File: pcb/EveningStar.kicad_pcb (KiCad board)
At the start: 2 copper layers, 134 parts, among them J1 3V3_JMP, J2 Connector, USB-TYPE-C-16P, J3 ESPPROG, J4 RJ45_Hanrun_HR911105A_Horizon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, Q1 SQ2308CES-T1_GE3-HXY, SW1 RST_SW, SW2 BOOT_SW, SW3 CFG_SW, U1 AMS1117S-5.0, U2 SN74HC132DR, U3 ISO6721RBDR, U4 DC-005H-D020, U5 LMR16010, U6 AHT20_C2757850, U7 TLV803SDBZR, U8 ESP32-C6-MINI-1, U9 W5500, Y1 25MHz

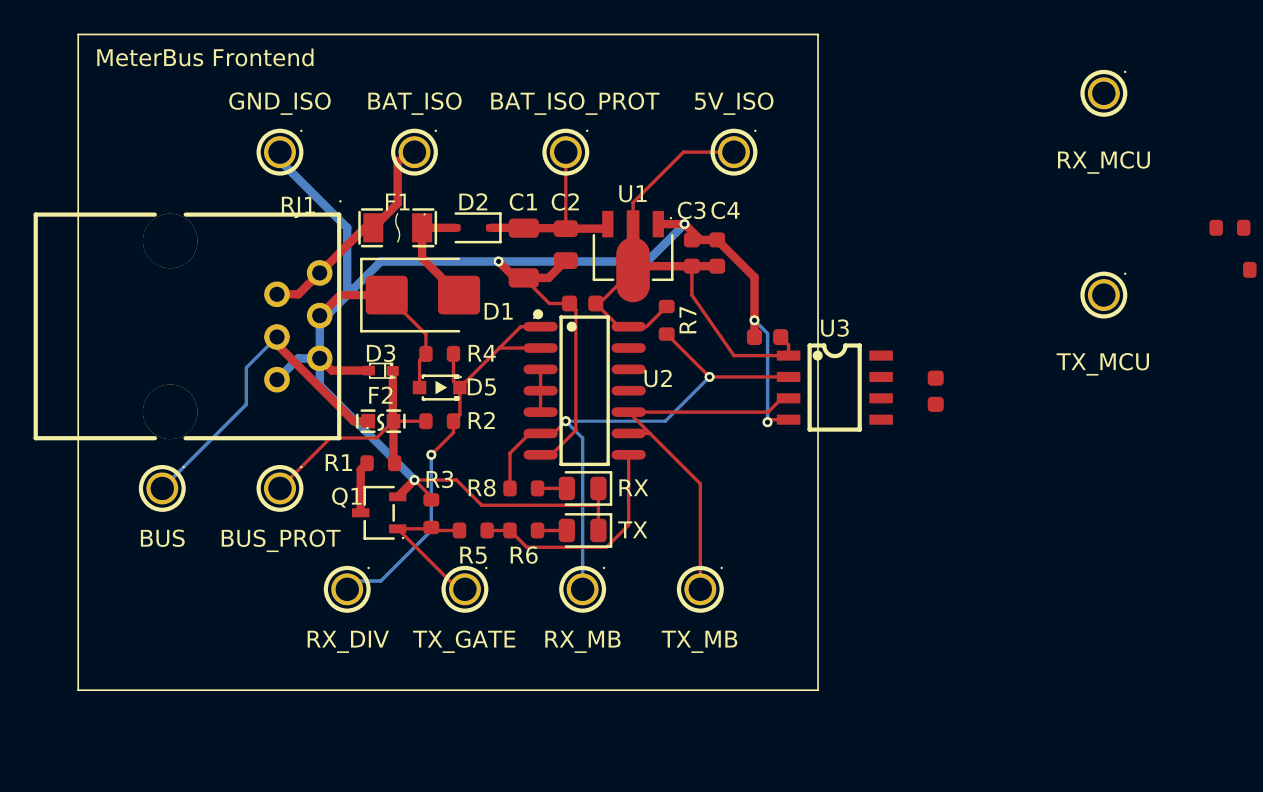
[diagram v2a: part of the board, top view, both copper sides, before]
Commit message: fix: flip rj11 meterbus connector
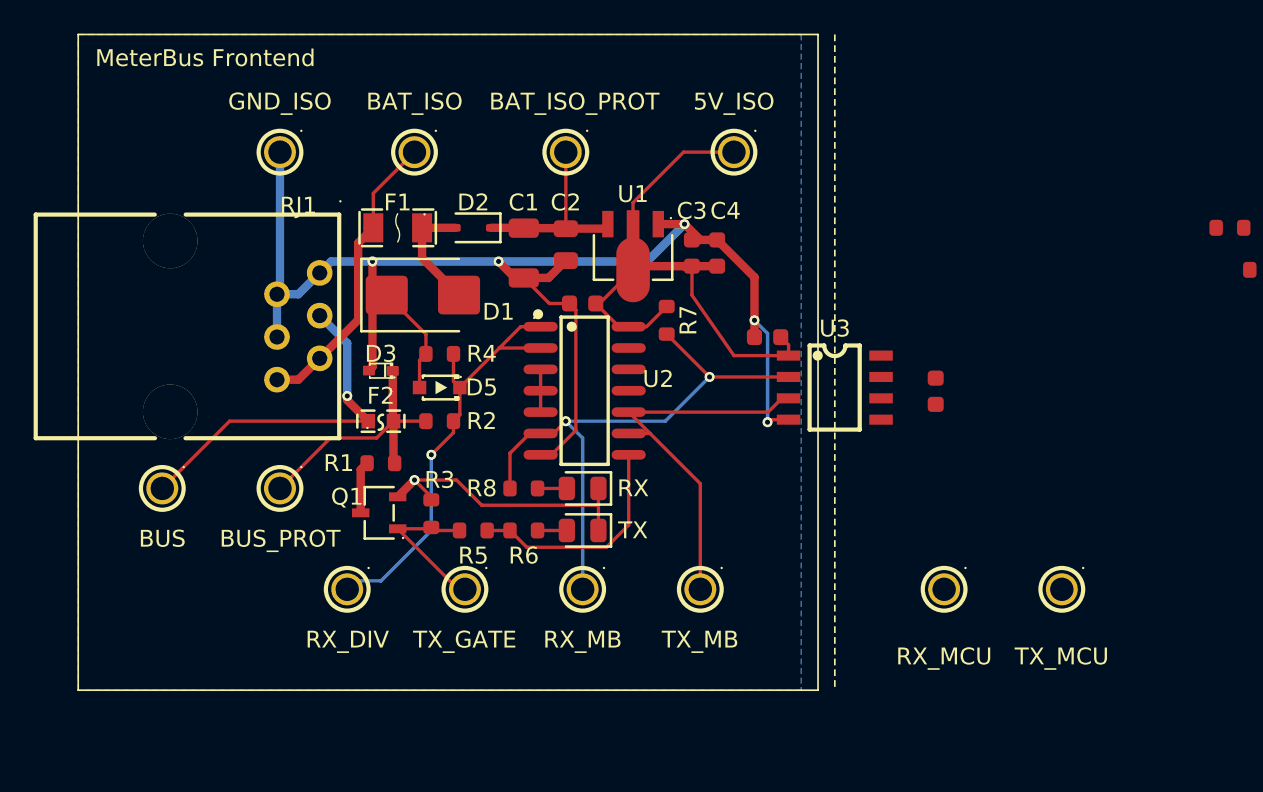
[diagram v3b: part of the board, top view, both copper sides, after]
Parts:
- moved TP17 31.0 mm to (-143.5, 54.0)
- moved TP16 17.7 mm to (-136.5, 54.0)
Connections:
- RJ1 pad 1: +BATT_ISO -> GND_ISO
- RJ1 pad 2: +BATT_ISO -> GND_ISO
- RJ1 pad 3: GND_ISO -> Net-(F2-Pad1)
- RJ1 pad 4: Net-(F2-Pad1) -> GND_ISO
- RJ1 pad 5: GND_ISO -> +BATT_ISO
- RJ1 pad 6: GND_ISO -> +BATT_ISO
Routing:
- net GND_ISO: track 117.6 -> 105.8 mm, vias 5 -> 6
- net +BATT_ISO: track 12.0 -> 18.2 mm
- net Net-(F2-Pad1): track 19.6 -> 21.8 mm, vias 0 -> 1
- added copper zone on B.Cu, net GND_ISO
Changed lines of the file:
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@@
 			(layers "*.Cu" "*.Mask")
 			(remove_unused_layers no)
-			(net "+BATT_ISO")
+			(net "GND_ISO")
 			(pinfunction "1_1")
 			(pintype "passive")
@@
 			(layers "*.Cu" "*.Mask")
 			(remove_unused_layers no)
-			(net "+BATT_ISO")
+			(net "GND_ISO")
 			(pinfunction "2_2")
 			(pintype "passive")
@@
 			(layers "*.Cu" "*.Mask")
 			(remove_unused_layers no)
-			(net "GND_ISO")
+			(net "Net-(F2-Pad1)")
 			(pinfunction "3_3")
 			(pintype "passive")
@@
 			(layers "*.Cu" "*.Mask")
 			(remove_unused_layers no)
-			(net "Net-(F2-Pad1)")
+			(net "GND_ISO")
 			(pinfunction "4_4")
 			(pintype "passive")
@@
 			(layers "*.Cu" "*.Mask")
 			(remove_unused_layers no)
-			(net "GND_ISO")
+			(net "+BATT_ISO")
 			(pinfunction "5_5")
 			(pintype "passive")
@@
 			(layers "*.Cu" "*.Mask")
 			(remove_unused_layers no)
-			(net "GND_ISO")
+			(net "+BATT_ISO")
 			(pinfunction "6_6")
 			(pintype "passive")
@@
 	(footprint "EasyEDA:TEST-TH_BD2.54-P1.4_BLACK"
 		(layer "F.Cu")
-		(at -134 24.5)
+		(at -143.5 54)
 		(property "Reference" "TP17"
 			(at 0 -4 0)
@@
 	(footprint "EasyEDA:TEST-TH_BD2.54-P1.4_BLACK"
 		(layer "F.Cu")
-		(at -134 36.5)
+		(at -136.5 54)
 		(property "Reference" "TP16"
 			(at 0 -4 0)
@@
 		(layer "F.SilkS")
 	)
+	(gr_line
+		(start -150 21)
+		(end -150 60)
+		(stroke
+			(width 0.1)
+			(type dash)
+		)
+		(layer "F.SilkS")
+	)
 	(gr_text "MeterBus Frontend"
 		(at -194 23 0)
@@
 	)
 	(segment
-		(start -179.91 40.99)
-		(end -180.6375 40.2625)
-		(width 0.5)
-		(layer "F.Cu")
-		(net "GND_ISO")
-	)
-	(segment
 		(start -165.4 44.545)
 		(end -166.855 46)
@@
 	)
 	(segment
+		(start -176.65 36.5)
+		(end -177.5 37.35)
+		(width 0.5)
+		(layer "F.Cu")
+		(net "GND_ISO")
+	)
+	(segment
 		(start -154.78 38)
 		(end -154.78 39)
@@
 	)
 	(segment
+		(start -177.5 35.65)
+		(end -176.65 36.5)
+		(width 0.5)
+		(layer "F.Cu")
+		(net "GND_ISO")
+	)
+	(segment
 		(start -166.98 37)
 		(end -168.5 35.48)
@@
 	)
 	(segment
+		(start -183.1775 38.9925)
+		(end -183.1775 39.436527)
+		(width 0.5)
+		(layer "F.Cu")
+		(net "GND_ISO")
+	)
+	(segment
 		(start -175 47.5)
 		(end -172.5 47.5)
@@
 	)
 	(segment
+		(start -177.5 37.35)
+		(end -177.5 40.78)
+		(width 0.5)
+		(layer "F.Cu")
+		(net "GND_ISO")
+	)
+	(segment
 		(start -171 49)
 		(end -164.06 49)
@@
 	)
 	(segment
-		(start -179.415 36.5)
-		(end -180.6375 37.7225)
+		(start -177.5 40.78)
+		(end -177.71 40.99)
 		(width 0.5)
 		(layer "F.Cu")
@@
 	)
 	(segment
-		(start -176.65 36.5)
-		(end -179.415 36.5)
-		(width 0.5)
-		(layer "F.Cu")
-		(net "GND_ISO")
-	)
-	(segment
 		(start -158 33.22)
 		(end -158.94 32.28)
@@
 	)
 	(segment
-		(start -177.71 40.99)
-		(end -179.91 40.99)
-		(width 0.5)
-		(layer "F.Cu")
-		(net "GND_ISO")
-	)
-	(segment
 		(start -165.4 37.38)
 		(end -165.4 44.545)
@@
 	)
 	(segment
+		(start -177.5 34.5)
+		(end -177.5 35.65)
+		(width 0.5)
+		(layer "F.Cu")
+		(net "GND_ISO")
+	)
+	(segment
 		(start -153.853282 43.91)
 		(end -154.003282 44.06)
@@
 		(net "GND_ISO")
 	)
+	(via
+		(at -177.5 34.5)
+		(size 0.6)
+		(drill 0.3)
+		(layers "F.Cu" "B.Cu")
+		(net "GND_ISO")
+	)
 	(segment
 		(start -170 34.5)
@@
 	)
 	(segment
-		(start -181.9075 40.2625)
-		(end -183.1775 41.5325)
+		(start -181.9075 36.4525)
+		(end -180.6375 35.1825)
 		(width 0.5)
 		(layer "B.Cu")
@@
 	)
 	(segment
-		(start -180.6375 37.7225)
-		(end -180.2225 37.7225)
+		(start -177.5 34.5)
+		(end -170 34.5)
 		(width 0.5)
 		(layer "B.Cu")
@@
 	)
 	(segment
-		(start -180.2225 37.7225)
-		(end -179 36.5)
+		(start -183.1775 36.4525)
+		(end -183.1775 38.9925)
 		(width 0.5)
 		(layer "B.Cu")
@@
 	)
 	(segment
-		(start -180.6375 41.8625)
-		(end -180.6375 40.2625)
-		(width 0.5)
+		(start -154 38.78)
+		(end -154.78 38)
+		(width 0.2)
 		(layer "B.Cu")
 		(net "GND_ISO")
 	)
 	(segment
-		(start -180.6375 40.2625)
-		(end -181.9075 40.2625)
-		(width 0.5)
+		(start -154.003282 44.06)
+		(end -154 44.056718)
+		(width 0.2)
 		(layer "B.Cu")
 		(net "GND_ISO")
 	)
 	(segment
-		(start -170 34.5)
-		(end -177 34.5)
+		(start -183 28)
+		(end -183 36.275)
 		(width 0.5)
 		(layer "B.Cu")
@@
 	)
 	(segment
-		(start -180.6375 37.7225)
-		(end -180.6375 40.2625)
-		(width 0.5)
+		(start -154 44.056718)
+		(end -154 38.78)
+		(width 0.2)
 		(layer "B.Cu")
 		(net "GND_ISO")
 	)
 	(segment
-		(start -179 36.5)
-		(end -179 32.5)
+		(start -179.955 34.5)
+		(end -180.6375 35.1825)
 		(width 0.5)
 		(layer "B.Cu")
@@
 	)
 	(segment
-		(start -177 34.5)
-		(end -179 36.5)
+		(start -161.16 34.5)
+		(end -158.94 32.28)
 		(width 0.5)
 		(layer "B.Cu")
@@
 	)
 	(segment
-		(start -154 38.78)
-		(end -154.78 38)
-		(width 0.2)
-		(layer "B.Cu")
-		(net "GND_ISO")
-	)
-	(segment
-		(start -179 32.5)
-		(end -183 28.5)
+		(start -183.1775 36.4525)
+		(end -181.9075 36.4525)
 		(width 0.5)
 		(layer "B.Cu")
@@
 	)
 	(segment
-		(start -154.003282 44.06)
-		(end -154 44.056718)
-		(width 0.2)
-		(layer "B.Cu")
-		(net "GND_ISO")
-	)
-	(segment
-		(start -175 47.5)
-		(end -180.6375 41.8625)
+		(start -177.5 34.5)
+		(end -179.955 34.5)
 		(width 0.5)
 		(layer "B.Cu")
@@
 	)
 	(segment
-		(start -154 44.056718)
-		(end -154 38.78)
-		(width 0.2)
-		(layer "B.Cu")
-		(net "GND_ISO")
-	)
-	(segment
-		(start -161.16 34.5)
-		(end -158.94 32.28)
+		(start -183 36.275)
+		(end -183.1775 36.4525)
 		(width 0.5)
 		(layer "B.Cu")
@@
 	)
 	(segment
-		(start -183.1775 36.4525)
-		(end -181.9075 36.4525)
+		(start -181.9075 41.5325)
+		(end -180.6375 40.2625)
 		(width 0.5)
 		(layer "F.Cu")
@@
 	)
 	(segment
-		(start -180.6375 35.1825)
-		(end -177.955 32.5)
+		(start -180.6375 40.2625)
+		(end -178.35 37.975)
 		(width 0.5)
 		(layer "F.Cu")
@@
 	)
 	(segment
-		(start -181.9075 36.4525)
-		(end -180.6375 35.1825)
-		(width 0.5)
+		(start -177.45 30.45)
+		(end -175 28)
+		(width 0.2)
 		(layer "F.Cu")
 		(net "+BATT_ISO")
 	)
 	(segment
-		(start -176 28.5)
-		(end -176 31.05)
-		(width 0.5)
+		(start -177.45 32.5)
+		(end -177.45 30.45)
+		(width 0.2)
 		(layer "F.Cu")
 		(net "+BATT_ISO")
 	)
 	(segment
-		(start -176 31.05)
+		(start -178.35 33.4)
 		(end -177.45 32.5)
 		(width 0.5)
@@
 	)
 	(segment
+		(start -178.35 37.975)
+		(end -178.35 33.4)
+		(width 0.5)
+		(layer "F.Cu")
+		(net "+BATT_ISO")
+	)
+	(segment
 		(start -177.955 32.5)
 		(end -177.45 32.5)
@@
 	)
 	(segment
-		(start -183.1775 38.9925)
-		(end -183.1775 39.436527)
+		(start -183.1775 41.5325)
+		(end -181.9075 41.5325)
 		(width 0.5)
 		(layer "F.Cu")
-		(net "Net-(F2-Pad1)")
+		(net "+BATT_ISO")
 	)
 	(segment
-		(start -183.1775 39.436527)
-		(end -178.614027 44)
+		(start -179 42.5)
+		(end -179 42.75)
 		(width 0.5)
 		(layer "F.Cu")
@@
 	)
 	(segment
-		(start -178.614027 44)
+		(start -179 42.75)
 		(end -177.75 44)
 		(width 0.5)
@@
 	(segment
 		(start -190 48)
-		(end -185 43)
+		(end -186 44)
 		(width 0.2)
-		(layer "B.Cu")
+		(layer "F.Cu")
 		(net "Net-(F2-Pad1)")
 	)
 	(segment
-		(start -185 43)
-		(end -185 40.815)
+		(start -186 44)
+		(end -177.75 44)
 		(width 0.2)
+		(layer "F.Cu")
+		(net "Net-(F2-Pad1)")
+	)
+	(via
+		(at -179 42.5)
+		(size 0.6)
+		(drill 0.3)
+		(layers "F.Cu" "B.Cu")
+		(net "Net-(F2-Pad1)")
+	)
+	(segment
+		(start -180.6375 37.7225)
+		(end -180.2225 37.7225)
+		(width 0.5)
 		(layer "B.Cu")
 		(net "Net-(F2-Pad1)")
 	)
 	(segment
-		(start -185 40.815)
-		(end -183.1775 38.9925)
-		(width 0.2)
+		(start -179 39.36)
+		(end -179 42.5)
+		(width 0.5)
+		(layer "B.Cu")
+		(net "Net-(F2-Pad1)")
+	)
+	(segment
+		(start -180.6375 37.7225)
+		(end -179 39.36)
+		(width 0.5)
 		(layer "B.Cu")
 		(net "Net-(F2-Pad1)")
@@
 			)
 		)
+	)
+	(zone
+		(net "GND_ISO")
+		(layer "B.Cu")
+		(name "GND_ISO")
+		(hatch edge 0.5)
+		(connect_pads
+			(clearance 0.5)
+		)
+		(min_thickness 0.25)
+		(fill yes
+			(thermal_gap 0.5)
+			(thermal_bridge_width 0.5)
+			(island_removal_mode 0)
+		)
+		(polygon
+			(pts
+				(xy -195 21) (xy -152 21) (xy -152 60) (xy -195 60)
+			)
+		)

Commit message: feat: layout ethernet
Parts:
- moved J4 363.4 mm to (27.5, 51.5)
- moved U9 363.1 mm to (-5.88, 49.4), turned to 90 degrees
- moved C10 267.9 mm to (-83.7, 2.19)
- moved C11 267.9 mm to (-95.2, 1.17)
- moved C8 267.9 mm to (-95.2, -5.53)
- moved C9 267.9 mm to (-95.2, -2.18)
- moved D10 267.9 mm to (-101.7, -1.19)
- moved D7 267.9 mm to (-85.5, -16.1)
- moved D8 267.9 mm to (-101.7, -5.20)
- moved D9 267.9 mm to (-101.7, 2.82)
- moved F3 267.9 mm to (-82.8, -5.54)
- moved J1 267.9 mm to (-89.2, 2.62)
- moved L1 267.9 mm to (-86.8, -11.1)
- moved R11 267.9 mm to (-82.2, -12.7)
- moved R12 267.9 mm to (-83.6, -2.64)
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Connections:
- net Net-(J4-RD+) renamed /ethernet/RD+
- net Net-(J4-RD-) renamed /ethernet/RD-
- net Net-(J4-TD+) renamed /ethernet/TD+
- net Net-(J4-TD-) renamed /ethernet/TD-
- net Net-(U9-RXN) renamed /ethernet/RXN
- net Net-(U9-RXP) renamed /ethernet/RXP
- net Net-(U9-TXN) renamed /ethernet/TXN
- net Net-(U9-TXP) renamed /ethernet/TXP
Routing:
- net GND: track 0.00 -> 95.4 mm, vias 0 -> 4
- net +3V3: track 0.00 -> 93.2 mm, vias 0 -> 3
- net +3V3A: track 0.00 -> 56.8 mm, vias 0 -> 6
- net Net-(J4-Pad11): track 0.00 -> 39.2 mm
- net Net-(J4-Pad10): track 0.00 -> 36.6 mm
- net CGND: track 0.00 -> 26.1 mm
- net Net-(J4-RCT): track 0.00 -> 21.5 mm, vias 0 -> 3
- net /ethernet/TD+: track 0.00 -> 20.7 mm
- net /ethernet/TD-: track 0.00 -> 20.5 mm
- net /ethernet/ACT_LED: track 0.00 -> 19.1 mm, vias 0 -> 2
- net /ethernet/LINK_LED: track 0.00 -> 18.6 mm, vias 0 -> 2
- net /ethernet/RD+: track 0.00 -> 17.9 mm
- net /ethernet/RD-: track 0.00 -> 17.8 mm
- net Net-(U9-XI/CLKIN): track 0.00 -> 9.95 mm
- net Net-(J4-TCT): track 0.00 -> 8.42 mm
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- added copper zone on F.Cu, net GND

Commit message: feat: roughly lay out mcu
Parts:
- added TP18: MOSI, TestPoint:TestPoint_Pad_1.0x1.0mm, F.Cu at (-108.8, 46.0)
- added TP19: SCK, TestPoint:TestPoint_Pad_1.0x1.0mm, F.Cu at (-108.8, 41.5)
- added TP20: MISO, TestPoint:TestPoint_Pad_1.0x1.0mm, F.Cu at (-108.8, 43.8)
- added TP21: ETH_CS, TestPoint:TestPoint_Pad_1.0x1.0mm, F.Cu at (-108.8, 39.2)
- added TP22: ETH_INT, TestPoint:TestPoint_Pad_1.0x1.0mm, F.Cu at (-108.8, 48.2)
- added TP23: ETH_RST, TestPoint:TestPoint_Pad_1.0x1.0mm, F.Cu at (-108.8, 50.5)
- TP10: value TestPoint -> 3V3
- TP11: value TestPoint -> MCU_RST
- moved TP11 99.8 mm to (-139.2, 36.5)
- moved D12 96.1 mm to (-136.0, 40.5)
- moved C17 88.3 mm to (-102.4, 42.3)
- moved C18 88.3 mm to (-105.4, 44.8)
- moved C19 88.3 mm to (-98.9, 42.7)
- moved C20 88.3 mm to (-98.9, 44.2)
- moved C21 88.3 mm to (-72.1, 45.2)
- moved C22 88.3 mm to (-94.4, 41.2)
- moved C23 88.3 mm to (-95.9, 41.2)
- moved C24 88.3 mm to (-86.1, 49.2)
- moved C25 88.3 mm to (-97.4, 40.4)
- moved C26 88.3 mm to (-86.9, 44.2)
- moved C27 88.3 mm to (-92.9, 41.2)
- moved C28 88.3 mm to (-91.4, 41.2)
- moved C29 88.3 mm to (-76.1, 50.2)
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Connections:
- net Net-(C31-Pad1) renamed /ethernet/RXP1
- net Net-(C32-Pad1) renamed /ethernet/RXN1
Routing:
- net GND: track 95.4 -> 197.7 mm, vias 4 -> 8
- net /mcu/IO9: track 0.00 -> 51.3 mm, vias 0 -> 6
- net ETH_RST: track 0.00 -> 46.4 mm, vias 0 -> 2
- net /mcu/MCU_RESET: track 0.00 -> 44.9 mm, vias 0 -> 1
- net MB_WRITE: track 0.00 -> 38.9 mm, vias 0 -> 4
- net MB_READ: track 0.00 -> 33.1 mm, vias 0 -> 2
- net MOSI: track 0.00 -> 27.5 mm
- net ETH_CS: track 0.00 -> 27.4 mm
- net SCK: track 0.00 -> 26.3 mm
- net +3V3: track 93.2 -> 118.9 mm
- net ETH_INT: track 0.00 -> 25.4 mm
- net MISO: track 0.00 -> 24.4 mm
- net /mcu/USB_D+: track 0.00 -> 18.1 mm
- net /mcu/USB_D-: track 0.00 -> 17.9 mm
- net Net-(U8-IO22): track 0.00 -> 17.8 mm, vias 0 -> 2
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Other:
- board text added: "Ethernet"
- board text added: "Power Supply"
- board text added: "Processor"

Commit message: feat: add filled zones
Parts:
- moved U4 231.7 mm to (173.1, 37.6)
- moved C1 231.6 mm to (63.0, 41.5)
- moved C10 231.6 mm to (139.3, 31.0)
- moved C11 231.6 mm to (144.3, 33.8)
- moved C12 231.6 mm to (90.2, 38.0)
- moved C13 231.6 mm to (122.0, 62.5)
- moved C14 231.6 mm to (93.8, 46.2)
- moved C15 231.6 mm to (92.5, 38.8)
- moved C16 231.6 mm to (92.5, 37.2)
- moved C17 231.6 mm to (129.1, 49.8)
- moved C18 231.6 mm to (126.1, 52.3)
- moved C19 231.6 mm to (132.6, 50.2)
- moved C2 231.6 mm to (65.5, 41.0)
- moved C20 231.6 mm to (132.6, 51.7)
- moved C21 231.6 mm to (159.4, 52.7)
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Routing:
- added copper zone on B.Cu, net GND
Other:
- board outline added: 145.5 x 40 mm

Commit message: feat: layout psu and rest of mcu
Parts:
- removed R11: 10kΩ, PCM_JLCPCB:R_0603
- moved TP10 34.8 mm to (130.0, 37.0)
- moved F3 28.0 mm to (166.0, 34.5)
- moved L1 23.1 mm to (137.8, 39.5), turned to -90 degrees
- moved TP9 22.7 mm to (134.0, 33.5), turned to 180 degrees
- moved U5 21.5 mm to (144.8, 33.5), turned to 90 degrees
- moved TP7 19.7 mm to (174.5, 42.5)
- moved J1 19.3 mm to (128.5, 41.0), turned to 0 degrees
- moved R16 18.6 mm to (107.0, 52.0), turned to 180 degrees
- moved R13 18.1 mm to (137.8, 32.5), turned to 90 degrees
- moved R15 17.0 mm to (107.0, 50.5), turned to 180 degrees
- moved C11 14.6 mm to (132.5, 42.5), turned to -90 degrees
- moved C10 11.4 mm to (149.3, 36.5), turned to -90 degrees
- moved C9 10.3 mm to (154.5, 36.0), turned to -90 degrees
- moved R12 9.55 mm to (146.8, 30.0)
- moved D9 8.88 mm to (159.5, 34.5), turned to 0 degrees
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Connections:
- U5 pad 6: Net-(U5-PGOOD) -> unconnected-(U5-PGOOD-Pad6)
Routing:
- net GND: track 197.7 -> 365.6 mm, vias 8 -> 12
- net +3V3: track 118.9 -> 239.8 mm, vias 3 -> 10
- net USB_PWR: track 0.00 -> 91.8 mm, vias 0 -> 4
- net /mcu/SDA: track 0.00 -> 56.8 mm, vias 0 -> 5
- net /mcu/SCL: track 0.00 -> 55.3 mm, vias 0 -> 7
- net Net-(U8-IO1): track 0.00 -> 32.4 mm, vias 0 -> 4
- net Net-(J1-Pin_2): track 0.00 -> 21.2 mm
- net Net-(D8-C): track 0.00 -> 19.4 mm
- net Net-(D10-C): track 0.00 -> 17.8 mm, vias 0 -> 2
- net /mcu/MCU_RESET: track 44.9 -> 61.9 mm, vias 1 -> 4
- net Net-(U5-FB): track 0.00 -> 8.89 mm
- net Net-(J2-CC2): track 0.00 -> 7.63 mm, vias 0 -> 2
- net Net-(D9-A): track 0.00 -> 6.83 mm
- net Net-(J2-CC1): track 0.00 -> 6.37 mm, vias 0 -> 2
- net /mcu/IO9: track 51.3 -> 54.3 mm, vias 6 -> 7
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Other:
- outline, holes or cut-outs redrawn

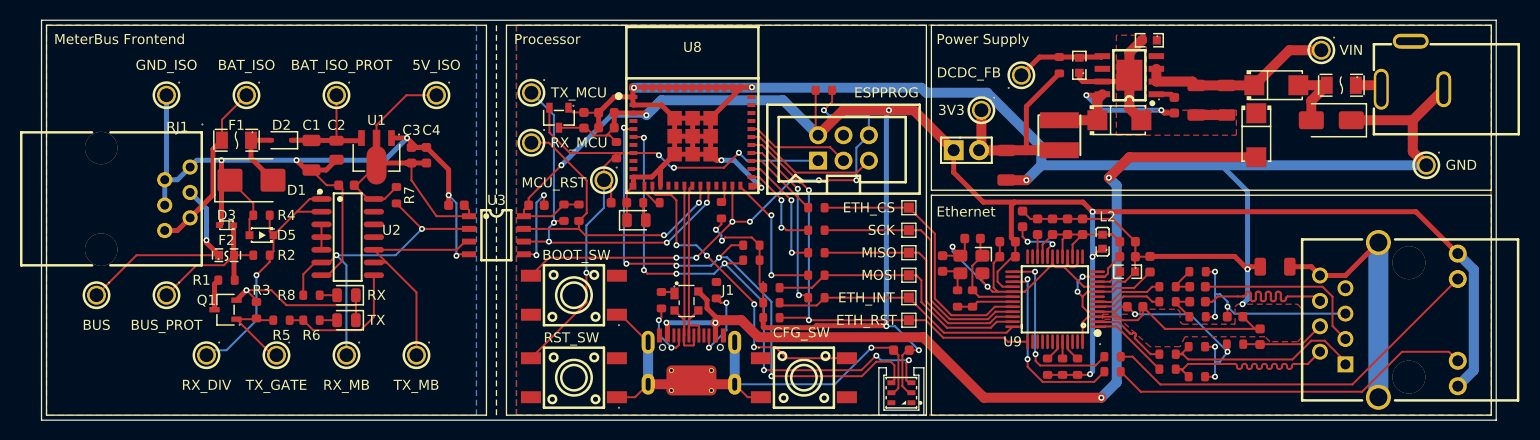
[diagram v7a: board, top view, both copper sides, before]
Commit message: fix: appease drc
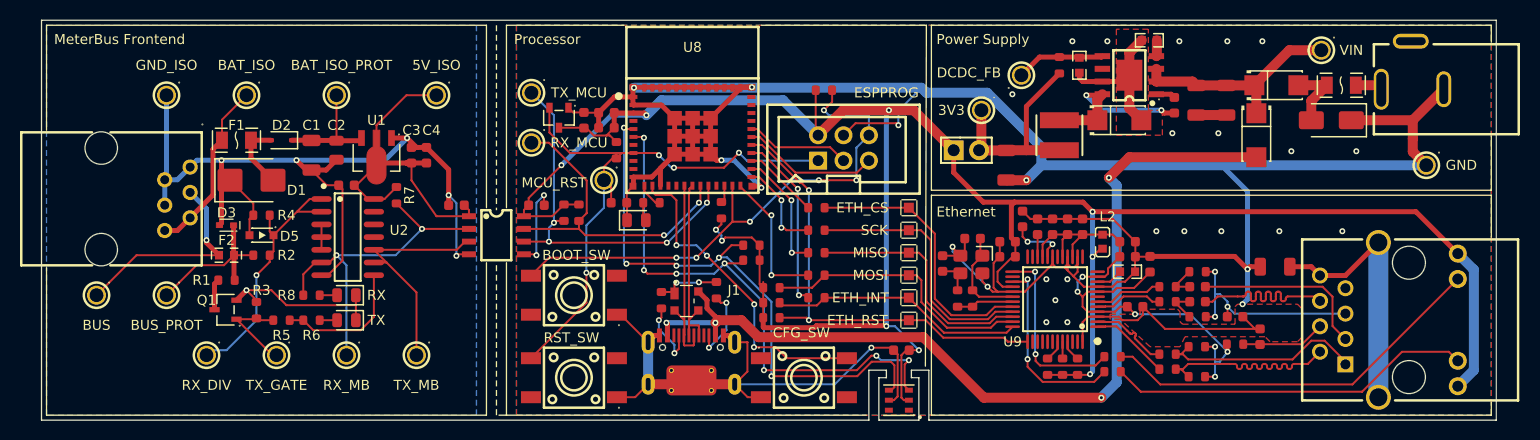
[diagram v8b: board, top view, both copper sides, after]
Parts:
- TP18, TP19, TP20, TP21, TP22, TP23: footprint TestPoint:TestPoint_Pad_1.0x1.0mm -> EasyEDA:TestPoint_Pad_1.0x1.0mm
- moved U6 0.79 mm to (121.8, 66.0)
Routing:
- net GND: track 365.6 -> 391.1 mm, vias 12 -> 35
- net Net-(D8-C): track 19.4 -> 22.3 mm
- net Net-(U5-RT/SYNC): track 0.00 -> 1.61 mm
- net /mcu/USB_D-: track 20.9 -> 19.3 mm
- net /mcu/USB_D+: track 21.0 -> 19.4 mm
- net /mcu/SDA: track 56.8 -> 57.8 mm
- net +3V3: track 239.8 -> 240.8 mm
- net Net-(J2-CC1): track 6.37 -> 7.19 mm
- net /mcu/SCL: track 55.3 -> 55.9 mm
- net /mcu/IO9: track 54.3 -> 54.2 mm, vias 7 -> 6
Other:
- outline, holes or cut-outs redrawn
